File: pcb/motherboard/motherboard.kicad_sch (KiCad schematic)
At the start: 15 parts, among them J3 UART_USB, J4 I2C_HEADER, SW2 GEN_MAZE, SW3 TOGGLE_MAZE, SW4 SOLVE_MAZE, U2 CH340C

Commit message: motherboard design update
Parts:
- removed J4: I2C_HEADER, symbol Connector:Conn_01x04_Pin
- added J4: I2C_HEADER, Connector:FanPinHeader_1x04_P2.54mm_Vertical, symbol Connector_Generic:Conn_01x04
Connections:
- net +5V: now also J4.1 (Pin_1)
- net GND: now also J4.4 (Pin_4)
- net STM32/I2C_SCL: now also J4.2 (Pin_2)
- net STM32/I2C_SDA: now also J4.3 (Pin_3)
- no-connect marks 9 -> 10
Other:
- moved on the sheet: C12, C13, C14, C15, R4, R5, R6, SW2, SW3, SW4

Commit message: motherboard schematic finished (pre-daughterboard connectors)
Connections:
- no-connect marks 10 -> 12
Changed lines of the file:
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@@
 	)
 	(no_connect
+		(at 68.58 99.06)
+	)
+	(no_connect
+		(at 68.58 96.52)
+	)
+	(no_connect
 		(at 116.84 173.99)
 	)
@@
 			)
 		)
-		(pin "MISO_0" output
+		(pin "MISO_0" input
 			(at 132.08 87.63 90)
 			(effects
@@
 			)
 		)
-		(pin "MISO_1" output
+		(pin "MISO_1" input
 			(at 147.32 92.71 0)
 			(effects
@@
 			)
 		)
-		(pin "MISO_2" output
+		(pin "MISO_2" input
 			(at 147.32 105.41 0)
 			(effects
@@
 			)
 		)
-		(pin "MISO_3" output
+		(pin "MISO_3" input
 			(at 147.32 118.11 0)
 			(effects
@@
 			)
 		)
-		(pin "MISO_4" output
+		(pin "MISO_4" input
 			(at 132.08 125.73 270)
 			(effects

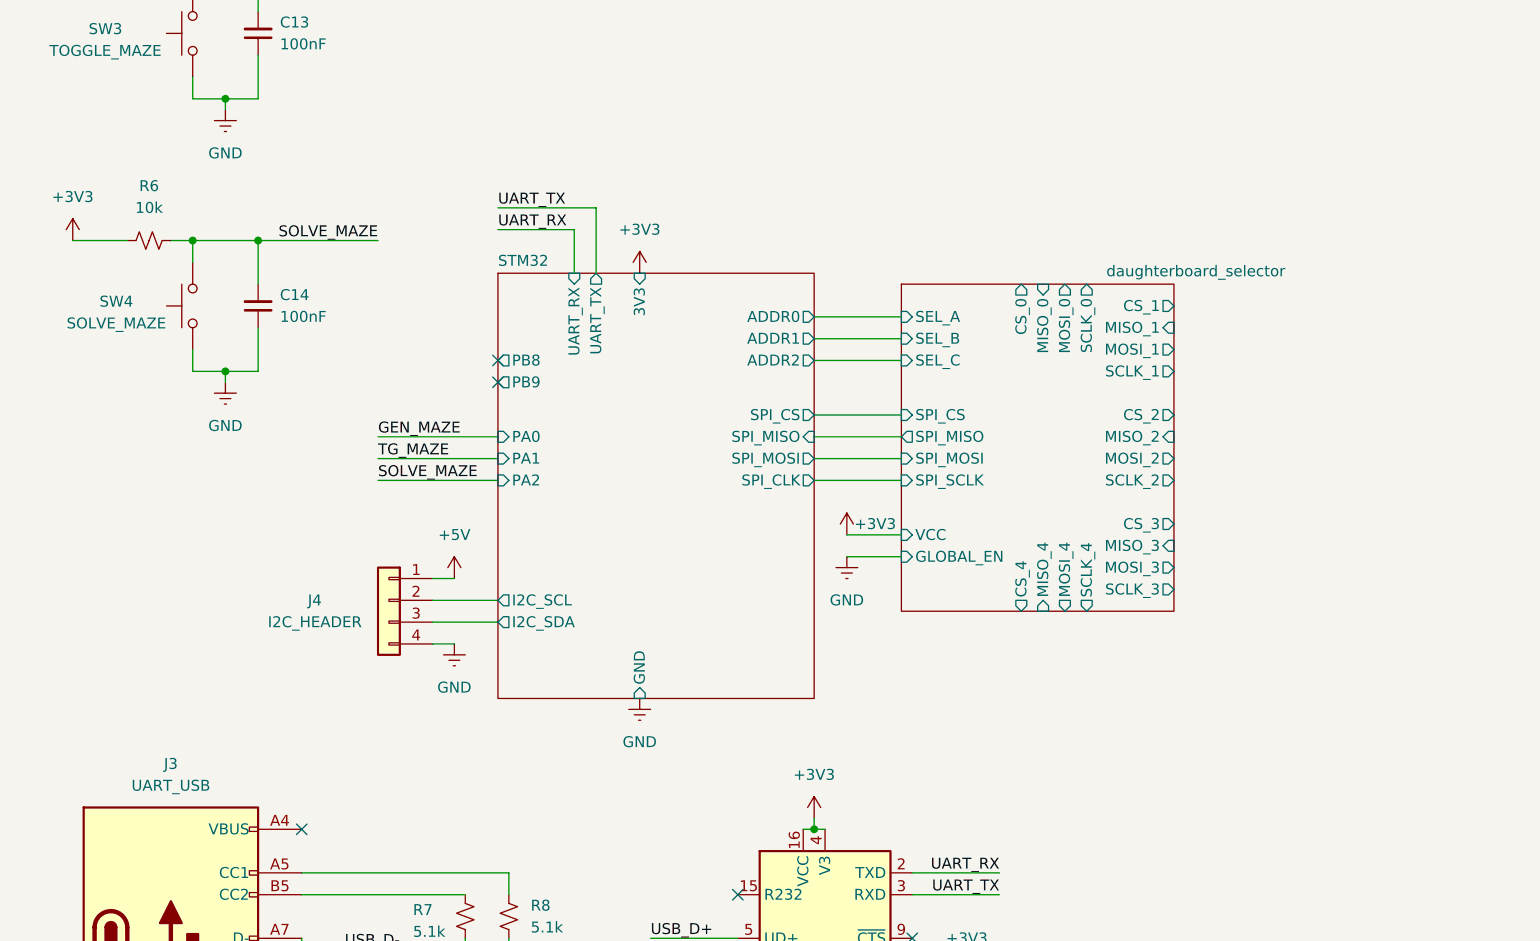
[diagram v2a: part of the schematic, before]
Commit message: added bidirectional voltage translator for I2C on motherboard
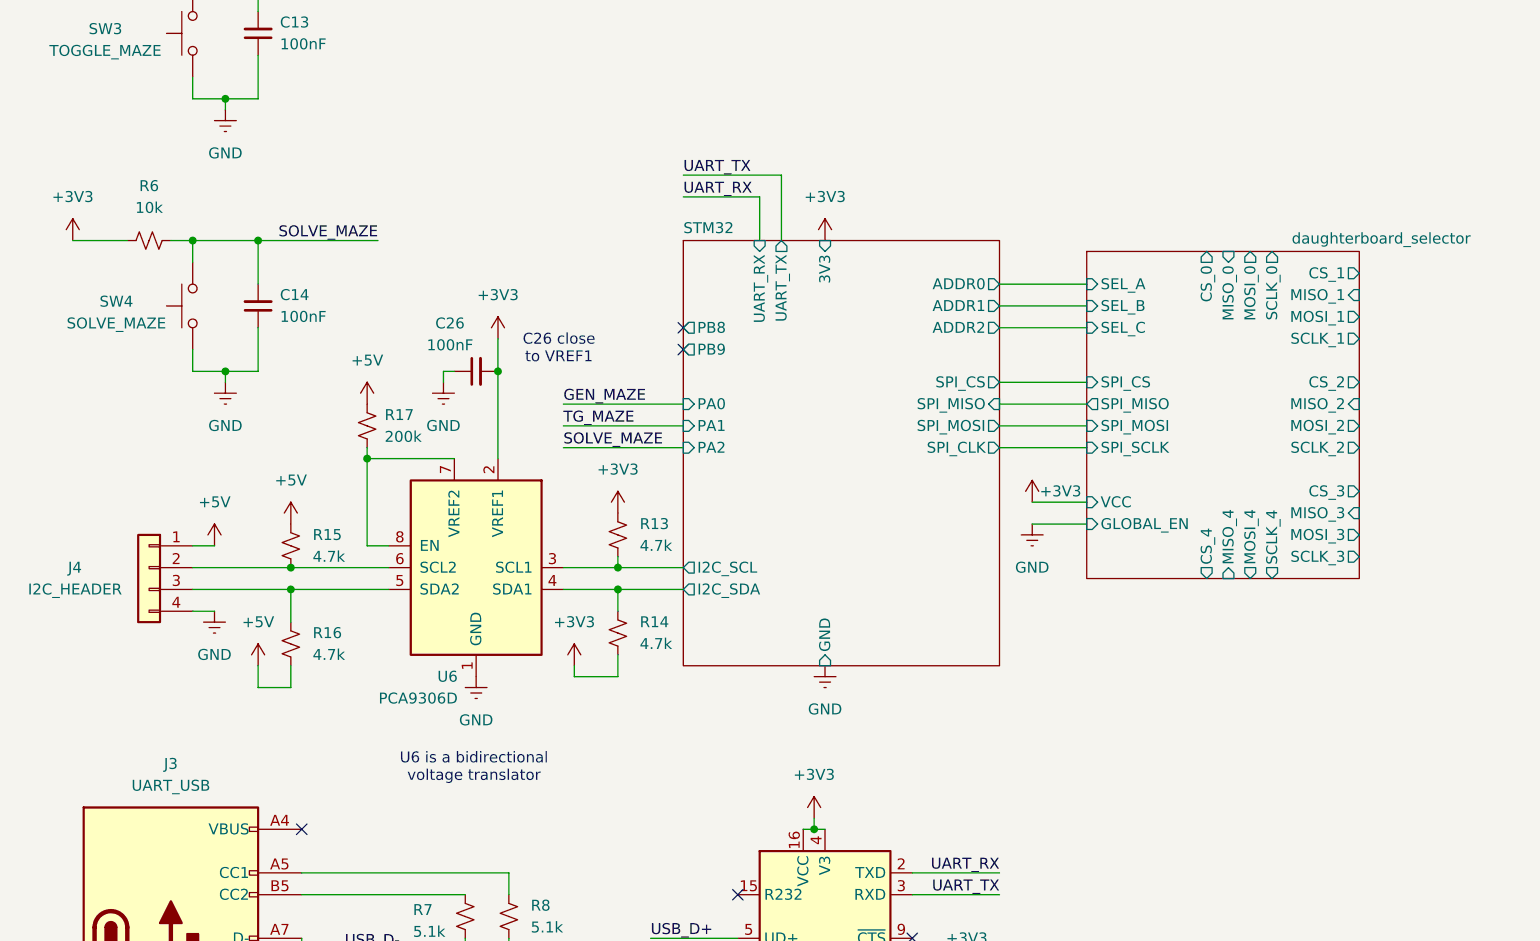
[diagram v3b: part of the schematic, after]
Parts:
- added C26: 100nF, Capacitor_SMD:C_0603_1608Metric, symbol Device:C_Small
- added R13, R14, R15, R16: 4.7k, symbol Device:R_Small_US
- added R17: 200k, symbol Device:R_Small_US
- added U6: PCA9306D, Package_SO:SO-8_3.9x4.9mm_P1.27mm, symbol Interface:PCA9306D
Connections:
- net +3V3: now also C26.2, R13.1, R14.2, U6.2 (VREF1)
- net +5V: now also R15.1, R16.2, R17.1
- net GND: now also C26.1, U6.1 (GND)
- net STM32/I2C_SCL: now also R13.2, U6.3 (SCL1); no longer J4.2 (Pin_2)
- net STM32/I2C_SDA: now also R14.1, U6.4 (SDA1); no longer J4.3 (Pin_3)
- new net: J4.3 (Pin_3), R16.1, U6.5 (SDA2)
- new net: J4.2 (Pin_2), R15.2, U6.6 (SCL2)
- new net: R17.2, U6.7 (VREF2), U6.8 (EN)
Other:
- note added: "C26 close to VREF1"
- note added: "U6 is a bidirectional voltage translator"

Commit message: added almost all footprints for PCB design
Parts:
- C12, C13, C14: footprint (none) -> Capacitor_SMD:C_0603_1608Metric
- J3: footprint Connector_USB:USB_C_Receptacle_Amphenol_12401948E412A -> Connector_USB:USB_C_Receptacle_HRO_TYPE-C-31-M-12
- J4: footprint Connector:FanPinHeader_1x04_P2.54mm_Vertical -> Connector_PinHeader_2.54mm:PinHeader_1x04_P2.54mm_Vertical
- R13, R14, R15, R16, R17, R4, R5, R6, R7, R8: footprint (none) -> Resistor_SMD:R_0603_1608Metric
- SW2, SW3, SW4: footprint (none) -> Connector_PinHeader_2.54mm:PinHeader_1x02_P2.54mm_Vertical
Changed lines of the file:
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@@
 			)
 		)
-		(property "Footprint" ""
+		(property "Footprint" "Connector_PinHeader_2.54mm:PinHeader_1x02_P2.54mm_Vertical"
 			(at 27.94 90.17 0)
 			(hide yes)
@@
 			)
 		)
-		(property "Footprint" ""
+		(property "Footprint" "Resistor_SMD:R_0603_1608Metric"
 			(at 27.94 50.8 0)
 			(hide yes)
@@
 			)
 		)
-		(property "Footprint" ""
+		(property "Footprint" "Resistor_SMD:R_0603_1608Metric"
 			(at 44.45 129.54 0)
 			(hide yes)
@@
 			)
 		)
-		(property "Footprint" ""
+		(property "Footprint" "Resistor_SMD:R_0603_1608Metric"
 			(at 82.55 128.27 0)
 			(hide yes)
@@
 			)
 		)
-		(property "Footprint" "Connector_USB:USB_C_Receptacle_Amphenol_12401948E412A"
+		(property "Footprint" "Connector_USB:USB_C_Receptacle_HRO_TYPE-C-31-M-12"
 			(at 34.29 166.37 0)
 			(hide yes)
@@
 			)
 		)
-		(property "Footprint" ""
+		(property "Footprint" "Capacitor_SMD:C_0603_1608Metric"
 			(at 40.64 30.48 0)
 			(hide yes)
@@
 			)
 		)
-		(property "Footprint" ""
+		(property "Footprint" "Resistor_SMD:R_0603_1608Metric"
 			(at 44.45 118.11 0)
 			(hide yes)
@@
 			)
 		)
-		(property "Footprint" ""
+		(property "Footprint" "Resistor_SMD:R_0603_1608Metric"
 			(at 69.85 161.29 0)
 			(hide yes)
@@
 			)
 		)
-		(property "Footprint" ""
+		(property "Footprint" "Resistor_SMD:R_0603_1608Metric"
 			(at 53.34 104.14 0)
 			(hide yes)
@@
 			)
 		)
-		(property "Footprint" ""
+		(property "Footprint" "Resistor_SMD:R_0603_1608Metric"
 			(at 64.77 161.29 0)
 			(hide yes)
@@
 			)
 		)
-		(property "Footprint" "Connector:FanPinHeader_1x04_P2.54mm_Vertical"
+		(property "Footprint" "Connector_PinHeader_2.54mm:PinHeader_1x04_P2.54mm_Vertical"
 			(at 27.94 120.65 0)
 			(hide yes)
@@
 			)
 		)
-		(property "Footprint" ""
+		(property "Footprint" "Connector_PinHeader_2.54mm:PinHeader_1x02_P2.54mm_Vertical"
 			(at 27.94 58.42 0)
 			(hide yes)
@@
 			)
 		)
-		(property "Footprint" ""
+		(property "Footprint" "Resistor_SMD:R_0603_1608Metric"
 			(at 27.94 22.86 0)
 			(hide yes)
@@
 			)
 		)
-		(property "Footprint" ""
+		(property "Footprint" "Connector_PinHeader_2.54mm:PinHeader_1x02_P2.54mm_Vertical"
 			(at 27.94 30.48 0)
 			(hide yes)
@@
 			)
 		)
-		(property "Footprint" ""
+		(property "Footprint" "Capacitor_SMD:C_0603_1608Metric"
 			(at 40.64 90.17 0)
 			(hide yes)
@@
 			)
 		)
-		(property "Footprint" ""
+		(property "Footprint" "Capacitor_SMD:C_0603_1608Metric"
 			(at 40.64 58.42 0)
 			(hide yes)
@@
 			)
 		)
-		(property "Footprint" ""
+		(property "Footprint" "Resistor_SMD:R_0603_1608Metric"
 			(at 82.55 116.84 0)
 			(hide yes)
@@
 			)
 		)
-		(property "Footprint" ""
+		(property "Footprint" "Resistor_SMD:R_0603_1608Metric"
 			(at 27.94 82.55 0)
 			(hide yes)

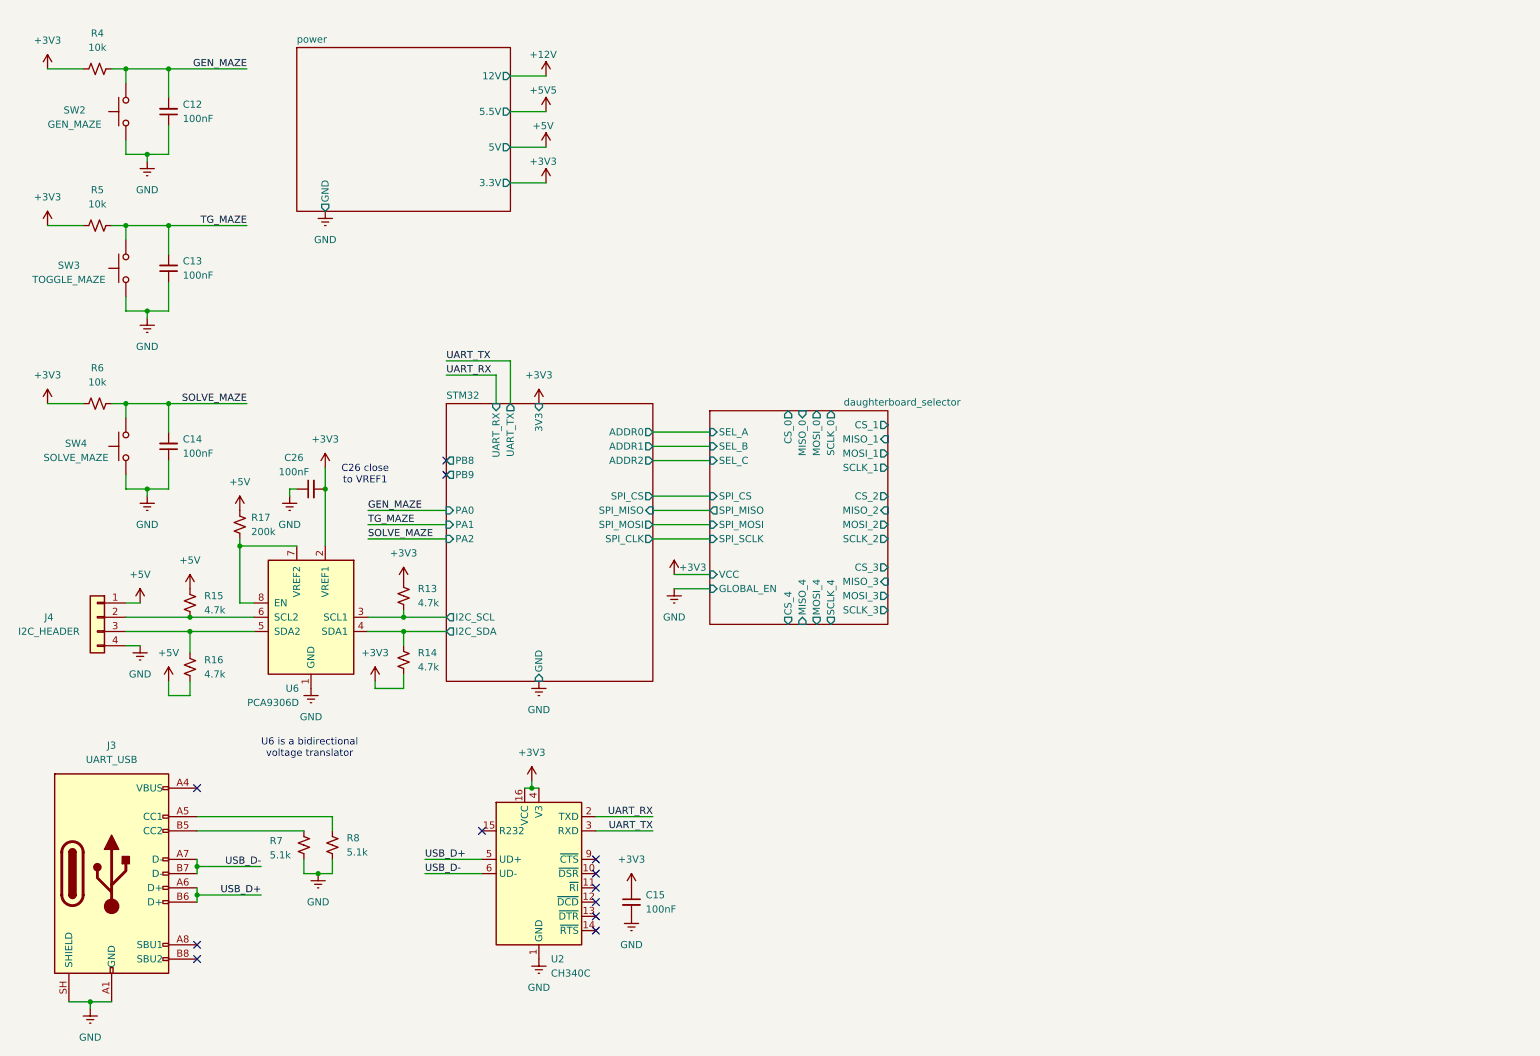
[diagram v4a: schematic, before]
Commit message: added testpoints, finished schematic, ready for PCB design
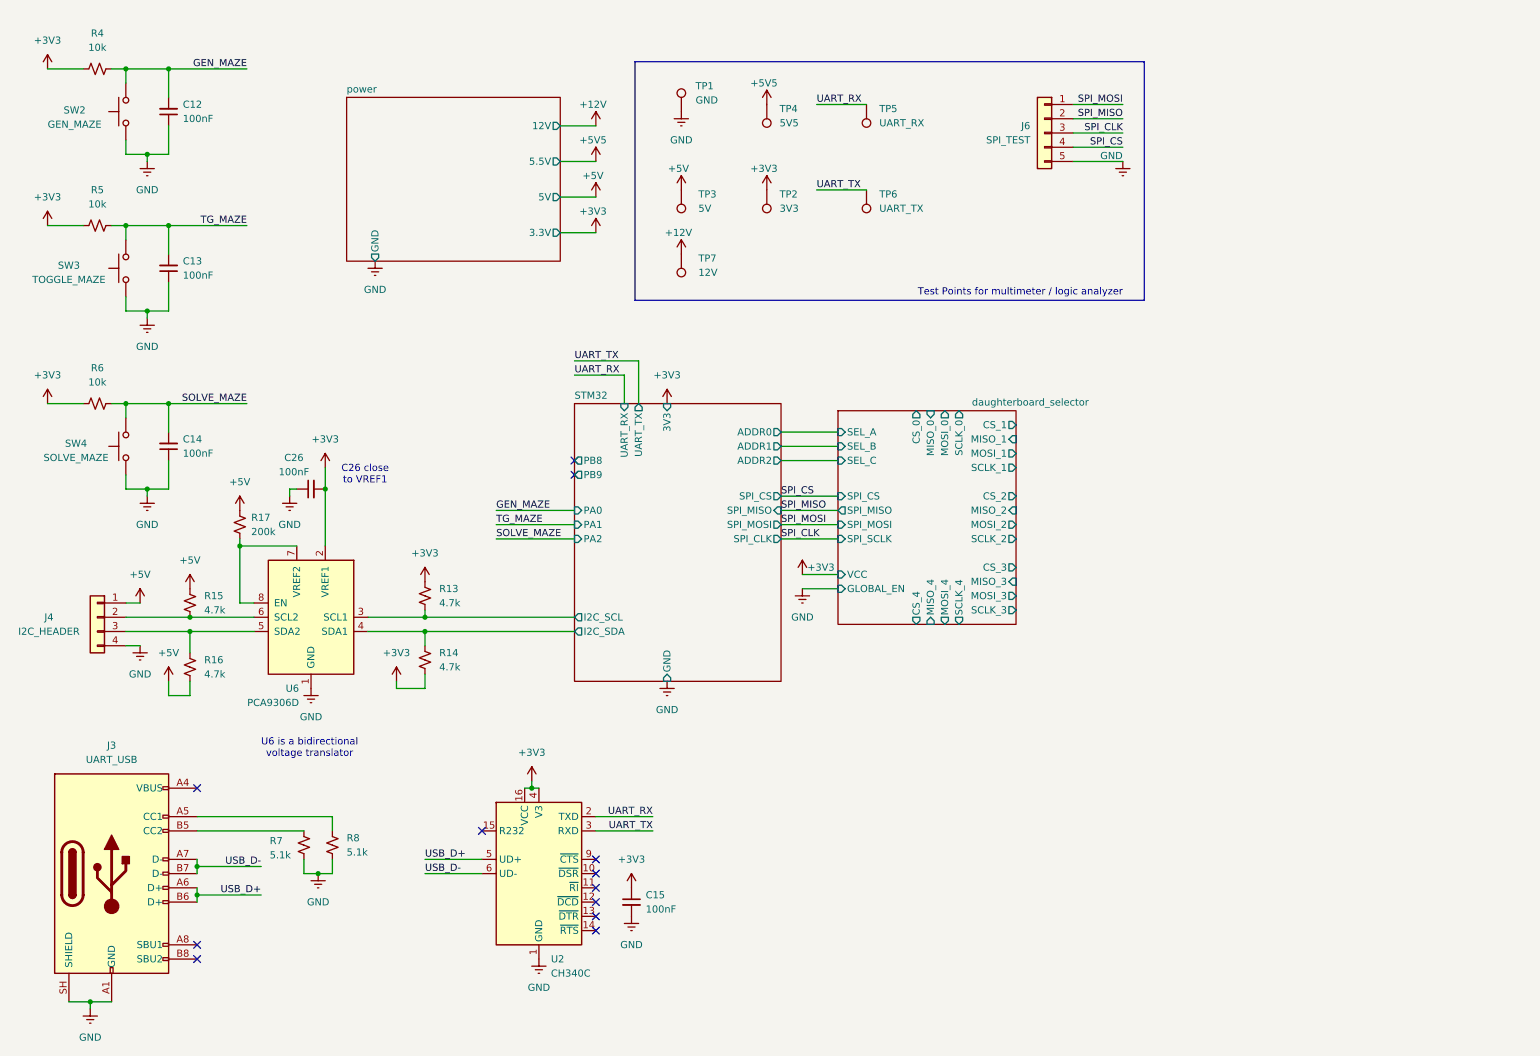
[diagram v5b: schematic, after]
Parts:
- added J6: SPI_TEST, Connector_PinHeader_2.54mm:PinHeader_1x05_P2.54mm_Vertical, symbol Connector_Generic:Conn_01x05
- added TP1: GND, TestPoint:TestPoint_Pad_2.0x2.0mm, symbol Connector:TestPoint
- added TP2: 3V3, TestPoint:TestPoint_Pad_2.0x2.0mm, symbol Connector:TestPoint
- added TP3: 5V, TestPoint:TestPoint_Pad_2.0x2.0mm, symbol Connector:TestPoint
- added TP4: 5V5, TestPoint:TestPoint_Pad_2.0x2.0mm, symbol Connector:TestPoint
- added TP5: UART_RX, TestPoint:TestPoint_Pad_2.0x2.0mm, symbol Connector:TestPoint
- added TP6: UART_TX, TestPoint:TestPoint_Pad_2.0x2.0mm, symbol Connector:TestPoint
- added TP7: 12V, TestPoint:TestPoint_Pad_2.0x2.0mm, symbol Connector:TestPoint
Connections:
- net +12V: now also TP7.1
- net +3V3: now also TP2.1
- net +5V: now also TP3.1
- net +5V5: now also TP4.1
- net GND: now also J6.5 (Pin_5), TP1.1
- net UART_RX: now also TP5.1
- net UART_TX: now also TP6.1
- new net SPI_CLK: J6.3 (Pin_3)
- new net SPI_CS: J6.4 (Pin_4)
- new net SPI_MISO: J6.2 (Pin_2)
- new net SPI_MOSI: J6.1 (Pin_1)
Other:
- note added: "Test Points for multimeter / logic analyzer"
- moved on the sheet: R13, R14
